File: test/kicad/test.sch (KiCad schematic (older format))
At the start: 5 parts, among them IC1 ATMEGA8-P, U1 74LS00, U2 NSL-32, U3 LAA110, U4 LP3966

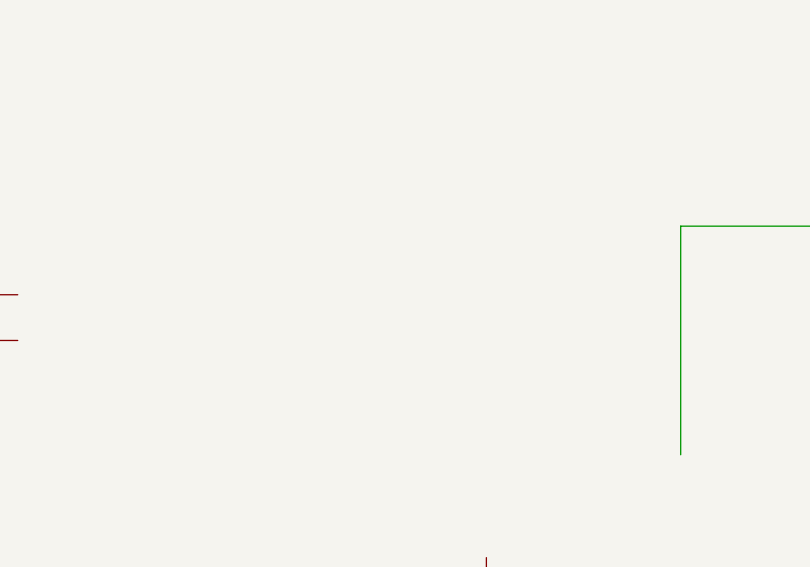
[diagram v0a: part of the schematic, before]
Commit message: Parse Text lines into design attribute annotations.
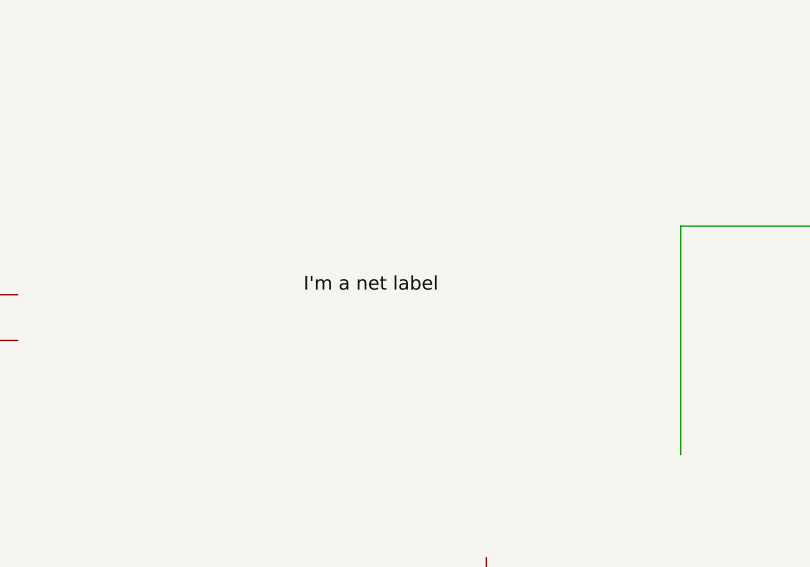
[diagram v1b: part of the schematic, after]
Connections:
- net labels added: I'm a net label
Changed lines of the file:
@@
-EESchema Schematic File Version 2  date Mon 12 Dec 2011 05:12:14 PM PST
+EESchema Schematic File Version 2  date Tue 20 Dec 2011 07:56:11 PM PST
 LIBS:power
 LIBS:device
@@
 Sheet 1 1
 Title ""
-Date "13 dec 2011"
+Date "21 dec 2011"
 Rev ""
 Comp ""
@@
 Comment4 ""
 $EndDescr
+Text Label 3350 2300 0    60   ~ 0
+I'm a net label
 $Comp
 L LAA110 U3
